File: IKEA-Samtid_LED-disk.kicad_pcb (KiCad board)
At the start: 2 copper layers, 100 x 100 mm, 70 parts

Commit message: Made schematic + placing a couple of LEDs.
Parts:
- removed C? (x2): VAL**, my_parts:MADW__C0805
- removed IC?: VAL**, my_parts:MADW__TQFP_32_7x7
- removed LED? (x63): VAL**, WS2812B:WS2812B_data-bridgeable
- removed P?: VAL**, my_parts:MADW__SIL-6
- removed X?: VAL**, my_parts:MADW__murata-resonator__CSTCE16M0V53-R0
- added C1: 100nF, my_parts:MADW__C0805, F.Cu at (186.0, 212.8)
- added C10: C, my_parts:MADW__C0805, F.Cu at (222.3, 182.1)
- added C11: C, my_parts:MADW__C0805, F.Cu at (237.5, 164.9)
- added C12: C, my_parts:MADW__C0805, F.Cu at (232.8, 170.3)
- added C13: C, my_parts:MADW__C0805, F.Cu at (245.2, 158.5)
- added C14: C, my_parts:MADW__C0805, F.Cu at (227.0, 175.7)
- added C15: C, my_parts:MADW__C0805, F.Cu at (210.0, 193.9)
- added C16: C, my_parts:MADW__C0805, F.Cu at (232.8, 163.9)
- added C17: C, my_parts:MADW__C0805, F.Cu at (217.6, 175.7)
- added C18: C, my_parts:MADW__C0805, F.Cu at (210.0, 187.5)
- added C19: C, my_parts:MADW__C0805, F.Cu at (245.2, 152.1)
- added C2: 1µF, my_parts:MADW__C0805, F.Cu at (193.3, 212.6)
- added C20: C, my_parts:MADW__C0805, F.Cu at (240.5, 158.5)
- added C21: C, my_parts:MADW__C0805, F.Cu at (224.1, 194.9)
- added C22: C, my_parts:MADW__C0805, F.Cu at (222.3, 175.7)
- added C23: C, my_parts:MADW__C0805, F.Cu at (240.5, 152.1)
- added C24: C, my_parts:MADW__C0805, F.Cu at (214.7, 194.9)
- added C25: C, my_parts:MADW__C0805, F.Cu at (227.0, 182.1)
- added C26: C, my_parts:MADW__C0805, F.Cu at (242.2, 164.9)
- added C27: C, my_parts:MADW__C0805, F.Cu at (237.5, 171.3)
- added C28: C, my_parts:MADW__C0805, F.Cu at (231.7, 176.7)
- added C29: C, my_parts:MADW__C0805, F.Cu at (219.4, 194.9)
- added C3: 100nF, my_parts:MADW__C0805, F.Cu at (186.0, 219.2)
- added C30: C, my_parts:MADW__C0805, F.Cu at (242.2, 171.3)
- added C31: C, my_parts:MADW__C0805, F.Cu at (217.6, 182.1)
- added C32: C, my_parts:MADW__C0805, F.Cu at (224.1, 188.5)
- added C33: C, my_parts:MADW__C0805, F.Cu at (231.7, 183.1)
- added C34: C, my_parts:MADW__C0805, F.Cu at (236.4, 177.8)
- added C35: C, my_parts:MADW__C0805, F.Cu at (241.1, 177.8)
- added C36: C, my_parts:MADW__C0805, F.Cu at (142.6, 57.9)
- added C37: C, my_parts:MADW__C0805, F.Cu at (339.0, 171.3)
- added C38: C, my_parts:MADW__C0805, F.Cu at (320.9, 189.6)
- added C39: C, my_parts:MADW__C0805, F.Cu at (302.1, 187.5)
- added C4: DNP, my_parts:MADW__C0805, F.Cu at (199.1, 205.2)
- added C40: C, my_parts:MADW__C0805, F.Cu at (316.2, 194.9)
- added C41: C, my_parts:MADW__C0805, F.Cu at (328.5, 184.2)
- added C42: C, my_parts:MADW__C0805, F.Cu at (333.2, 177.8)
- added C43: C, my_parts:MADW__C0805, F.Cu at (328.5, 177.8)
- added C44: C, my_parts:MADW__C0805, F.Cu at (323.8, 183.1)
- added C45: C, my_parts:MADW__C0805, F.Cu at (311.5, 188.5)
- added C46: C, my_parts:MADW__C0805, F.Cu at (332.5, 152.1)
- added C47: C, my_parts:MADW__C0805, F.Cu at (309.7, 175.7)
- added C48: C, my_parts:MADW__C0805, F.Cu at (324.9, 163.9)
- added C49: C, my_parts:MADW__C0805, F.Cu at (337.2, 152.1)
- added C5: C, my_parts:MADW__C0805, F.Cu at (150.0, 57.2)
- added C50: C, my_parts:MADW__C0805, F.Cu at (332.5, 158.5)
- added C51: C, my_parts:MADW__C0805, F.Cu at (314.4, 175.7)
- added C52: C, my_parts:MADW__C0805, F.Cu at (309.7, 182.1)
- added C53: C, my_parts:MADW__C0805, F.Cu at (302.1, 193.9)
- added C54: C, my_parts:MADW__C0805, F.Cu at (319.1, 175.7)
- added C55: C, my_parts:MADW__C0805, F.Cu at (337.2, 158.5)
- added C56: C, my_parts:MADW__C0805, F.Cu at (324.9, 170.3)
- added C57: C, my_parts:MADW__C0805, F.Cu at (329.6, 164.9)
- added C58: C, my_parts:MADW__C0805, F.Cu at (314.4, 182.1)
- added C59: C, my_parts:MADW__C0805, F.Cu at (306.8, 188.5)
- added C6: C, my_parts:MADW__C0805, F.Cu at (157.3, 57.9)
- added C60: C, my_parts:MADW__C0805, F.Cu at (306.8, 194.9)
- added C61: C, my_parts:MADW__C0805, F.Cu at (319.1, 182.1)
- added C62: C, my_parts:MADW__C0805, F.Cu at (334.3, 164.9)
- added C63: C, my_parts:MADW__C0805, F.Cu at (329.6, 171.3)
- added C64: C, my_parts:MADW__C0805, F.Cu at (323.8, 176.7)
- added C65: C, my_parts:MADW__C0805, F.Cu at (311.5, 194.9)
- added C66: C, my_parts:MADW__C0805, F.Cu at (334.3, 171.3)
- added C67: C, my_parts:MADW__C0805, F.Cu at (339.0, 164.9)
- added C68: C, my_parts:MADW__C0805, F.Cu at (316.2, 188.5)
- added C7: C, my_parts:MADW__C0805, F.Cu at (164.5, 59.7)
- added C8: C, my_parts:MADW__C0805, F.Cu at (219.4, 188.5)
- added C9: C, my_parts:MADW__C0805, F.Cu at (214.7, 188.5)
- added IC1: ATMEGA168PA-A, my_parts:MADW__TQFP_32_7x7, F.Cu at (168.4, 210.7)
- added JP1: AVR_ISP, my_parts:MADW__PIN_ARRAY_3x2_2.54mm, F.Cu at (179.2, 214.7)
- added LED1: WS2812B, WS2812B:WS2812B_data-bridgeable, F.Cu at (150.0, 50.0)
- added LED10: WS2812B, WS2812B:WS2812B_data-bridgeable, F.Cu at (198.7, 118.5)
- added LED11: WS2812B, WS2812B:WS2812B_data-bridgeable, F.Cu at (193.9, 130.0)
- added LED12: WS2812B, WS2812B:WS2812B_data-bridgeable, F.Cu at (186.7, 136.1)
- added LED13: WS2812B, WS2812B:WS2812B_data-bridgeable, F.Cu at (178.2, 138.4)
- added LED14: WS2812B, WS2812B:WS2812B_data-bridgeable, F.Cu at (169.7, 140.4)
- added LED15: WS2812B, WS2812B:WS2812B_data-bridgeable, F.Cu at (160.1, 143.9)
- added LED16: WS2812B, WS2812B:WS2812B_data-bridgeable, F.Cu at (150.0, 140.0)
- added LED17: WS2812B, WS2812B:WS2812B_data-bridgeable, F.Cu at (140.6, 143.1)
- added LED18: WS2812B, WS2812B:WS2812B_data-bridgeable, F.Cu at (132.5, 142.4)
- added LED19: WS2812B, WS2812B:WS2812B_data-bridgeable, F.Cu at (124.6, 138.4)
- added LED2: WS2812B, WS2812B:WS2812B_data-bridgeable, F.Cu at (158.8, 50.9)
- added LED20: WS2812B, WS2812B:WS2812B_data-bridgeable, F.Cu at (117.0, 134.3)
- added LED21: WS2812B, WS2812B:WS2812B_data-bridgeable, F.Cu at (109.7, 126.2)
- added LED22: WS2812B, WS2812B:WS2812B_data-bridgeable, F.Cu at (104.2, 117.9)
- added LED23: WS2812B, WS2812B:WS2812B_data-bridgeable, F.Cu at (100.6, 105.7)
- added LED24: WS2812B, WS2812B:WS2812B_data-bridgeable, F.Cu at (105.0, 95.0)
- added LED25: WS2812B, WS2812B:WS2812B_data-bridgeable, F.Cu at (101.2, 84.3)
- added LED26: WS2812B, WS2812B:WS2812B_data-bridgeable, F.Cu at (103.6, 72.7)
- added LED27: WS2812B, WS2812B:WS2812B_data-bridgeable, F.Cu at (111.6, 65.6)
- added LED28: WS2812B, WS2812B:WS2812B_data-bridgeable, F.Cu at (117.0, 57.5)
- added LED29: WS2812B, WS2812B:WS2812B_data-bridgeable, F.Cu at (123.5, 52.4)
- added LED3: WS2812B, WS2812B:WS2812B_data-bridgeable, F.Cu at (167.2, 53.4)
- added LED30: WS2812B, WS2812B:WS2812B_data-bridgeable, F.Cu at (131.1, 49.2)
- added LED31: WS2812B, WS2812B:WS2812B_data-bridgeable, F.Cu at (137.4, 40.7)
- added LED32: WS2812B, WS2812B:WS2812B_data-bridgeable, F.Cu at (141.3, 50.9)
- added LED33: WS2812B, WS2812B:WS2812B_data-bridgeable, F.Cu at (257.9, 178.5)
- added LED34: WS2812B, WS2812B:WS2812B_data-bridgeable, F.Cu at (265.5, 154.9)
- added LED35: WS2812B, WS2812B:WS2812B_data-bridgeable, F.Cu at (257.9, 166.7)
- added LED36: WS2812B, WS2812B:WS2812B_data-bridgeable, F.Cu at (280.7, 178.5)
- added LED37: WS2812B, WS2812B:WS2812B_data-bridgeable, F.Cu at (265.5, 190.3)
- added LED38: WS2812B, WS2812B:WS2812B_data-bridgeable, F.Cu at (295.9, 166.7)
- added LED39: WS2812B, WS2812B:WS2812B_data-bridgeable, F.Cu at (303.5, 166.7)
- added LED4: WS2812B, WS2812B:WS2812B_data-bridgeable, F.Cu at (175.0, 57.6)
- added LED40: WS2812B, WS2812B:WS2812B_data-bridgeable, F.Cu at (273.1, 190.3)
- added LED41: WS2812B, WS2812B:WS2812B_data-bridgeable, F.Cu at (288.3, 178.5)
- added LED42: WS2812B, WS2812B:WS2812B_data-bridgeable, F.Cu at (311.2, 154.9)
- added LED43: WS2812B, WS2812B:WS2812B_data-bridgeable, F.Cu at (280.7, 190.3)
- added LED44: WS2812B, WS2812B:WS2812B_data-bridgeable, F.Cu at (295.9, 178.5)
- added LED45: WS2812B, WS2812B:WS2812B_data-bridgeable, F.Cu at (311.2, 166.7)
- added LED46: WS2812B, WS2812B:WS2812B_data-bridgeable, F.Cu at (295.9, 190.3)
- added LED47: WS2812B, WS2812B:WS2812B_data-bridgeable, F.Cu at (318.8, 166.7)
- added LED48: WS2812B, WS2812B:WS2812B_data-bridgeable, F.Cu at (288.3, 190.3)
- added LED49: WS2812B, WS2812B:WS2812B_data-bridgeable, F.Cu at (326.4, 154.9)
- added LED5: WS2812B, WS2812B:WS2812B_data-bridgeable, F.Cu at (183.4, 65.0)
- added LED51: WS2812B, WS2812B:WS2812B_data-bridgeable, F.Cu at (318.8, 154.9)
- added LED52: WS2812B, WS2812B:WS2812B_data-bridgeable, F.Cu at (257.9, 154.9)
- added LED53: WS2812B, WS2812B:WS2812B_data-bridgeable, F.Cu at (273.1, 178.5)
- added LED54: WS2812B, WS2812B:WS2812B_data-bridgeable, F.Cu at (288.3, 166.7)
- added LED55: WS2812B, WS2812B:WS2812B_data-bridgeable, F.Cu at (280.7, 166.7)
- added LED56: WS2812B, WS2812B:WS2812B_data-bridgeable, F.Cu at (303.5, 154.9)
- added LED57: WS2812B, WS2812B:WS2812B_data-bridgeable, F.Cu at (295.9, 154.9)
- added LED58: WS2812B, WS2812B:WS2812B_data-bridgeable, F.Cu at (288.3, 154.9)
- added LED6: WS2812B, WS2812B:WS2812B_data-bridgeable, F.Cu at (189.6, 73.5)
- added LED60: WS2812B, WS2812B:WS2812B_data-bridgeable, F.Cu at (265.5, 178.5)
- added LED61: WS2812B, WS2812B:WS2812B_data-bridgeable, F.Cu at (273.1, 166.7)
- added LED62: WS2812B, WS2812B:WS2812B_data-bridgeable, F.Cu at (257.9, 190.3)
- added LED63: WS2812B, WS2812B:WS2812B_data-bridgeable, F.Cu at (265.5, 166.7)
- added LED64: WS2812B, WS2812B:WS2812B_data-bridgeable, F.Cu at (273.1, 154.9)
- added LED7: WS2812B, WS2812B:WS2812B_data-bridgeable, F.Cu at (194.1, 85.5)
- added LED8: WS2812B, WS2812B:WS2812B_data-bridgeable, F.Cu at (195.0, 95.0)
- added LED9: WS2812B, WS2812B:WS2812B_data-bridgeable, F.Cu at (203.8, 107.1)
- added P1: FTDI, my_parts:MADW__SIL-6, F.Cu at (183.0, 205.8)
- added P2: POWER, my_parts:MADW__SIL-2, F.Cu at (193.9, 205.8)
- added R1: 10k, my_parts:MADW__R0603_2, F.Cu at (190.7, 219.0)
- LED50: renamed from P?; value VAL** -> WS2812B; footprint my_parts:MADW__PIN_ARRAY_3x2_2.54mm -> WS2812B:WS2812B_data-bridgeable; moved to F.Cu
- LED59: renamed from LED?; value VAL** -> WS2812B; moved to F.Cu
- moved LED50 148.1 mm to (303.5, 178.5), turned to 0 degrees
- moved LED59 98.7 mm to (280.7, 154.9), turned to 0 degrees
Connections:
- LED50 pad 1: (no net) -> +5V
- LED50 pad 2: (no net) -> Net-(LED50-Pad2)
- LED50 pad 3: (no net) -> GND
- LED50 pad 4: (no net) -> Net-(LED49-Pad2)
- LED59 pad 1: (no net) -> +5V
- LED59 pad 2: (no net) -> Net-(LED59-Pad2)
- LED59 pad 3: (no net) -> GND
- LED59 pad 4: (no net) -> Net-(LED58-Pad2)
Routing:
- net GND: track 0.00 -> 44.7 mm
- net +5V: track 0.00 -> 20.5 mm
- net Net-(LED2-Pad2): track 0.00 -> 11.4 mm, vias 0 -> 2
- net Net-(LED1-Pad2): track 0.00 -> 11.2 mm, vias 0 -> 2
- net Net-(LED3-Pad2): track 0.00 -> 10.9 mm, vias 0 -> 2
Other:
- net class Default: clearance 0.254 -> 0.2032; trace_width 0.254 -> 0.4064; via_drill 0.635 -> 0.508
- rule trace_clearance: 0.254 -> 0.2032
- board text removed: "fix the angles!"

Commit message: First serious attempt at routing the board. No fun so far.
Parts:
- C1, C2, C3, C37, C38, C39, C4, C40, C68, IC1, JP1, LED33, LED34, LED35, LED36, LED37, LED38, LED39, LED40, LED41, LED64, P1, P2, R1: moved to B.Cu
- moved C37 220.8 mm to (150.0, 57.2), turned to 180 degrees
- moved C68 217.2 mm to (142.6, 57.9), turned to 191.3 degrees
- moved C38 209.9 mm to (157.4, 57.9), turned to 168.7 degrees
- moved C40 195.8 mm to (171.0, 63.6), turned to 146.7 degrees
- moved C39 187.6 mm to (164.4, 60.0), turned to 157.5 degrees
- moved LED64 167.9 mm to (141.3, 50.9), turned to 11.3 degrees
- moved LED33 167.7 mm to (150.0, 50.0)
- moved LED36 160.6 mm to (175.0, 57.6), turned to 326.2 degrees
- moved LED37 152.1 mm to (181.8, 63.2), turned to 315 degrees
- moved LED34 149.0 mm to (158.8, 50.9), turned to 348.7 degrees
- moved LED38 145.3 mm to (187.4, 70.0), turned to 303.8 degrees
- moved LED35 145.1 mm to (167.2, 53.4), turned to 337.5 degrees
- moved LED39 142.9 mm to (191.6, 77.8), turned to 292.4 degrees
- moved C8 134.0 mm to (171.0, 63.6), turned to 326.2 degrees
- moved LED40 130.6 mm to (194.1, 86.2), turned to 281.2 degrees
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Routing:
- net GND: track 44.7 -> 166.7 mm
- net +5V: track 20.5 -> 76.2 mm
- net Net-(LED39-Pad2): track 0.00 -> 20.2 mm, vias 0 -> 11
- net Net-(LED35-Pad2): track 0.00 -> 20.1 mm, vias 0 -> 10
- net Net-(LED33-Pad2): track 0.00 -> 19.7 mm, vias 0 -> 5
- net Net-(LED37-Pad2): track 0.00 -> 19.5 mm, vias 0 -> 10
- net /WS2812B-LEDs-1/D_OUT: track 0.00 -> 17.3 mm, vias 0 -> 1
- net Net-(LED36-Pad2): track 0.00 -> 17.1 mm
- net Net-(LED38-Pad2): track 0.00 -> 16.5 mm
- net /WS2812B-LEDs-2/E_OUT: track 0.00 -> 16.4 mm
- net Net-(LED34-Pad2): track 0.00 -> 16.2 mm
- net /WS2812B-LEDs-1/A_OUT: track 0.00 -> 11.3 mm, vias 0 -> 7
- net Net-(LED5-Pad2): track 0.00 -> 11.2 mm, vias 0 -> 5
- net Net-(LED4-Pad2): track 0.00 -> 11.1 mm, vias 0 -> 4
- net Net-(LED6-Pad2): track 0.00 -> 11.1 mm, vias 0 -> 4
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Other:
- net class Default: via_dia 0.889 -> 0.7112; via_drill 0.508 -> 0.3302
- rule via_min_drill: 0.508 -> 0.3302
- rule via_min_size: 0.889 -> 0.635

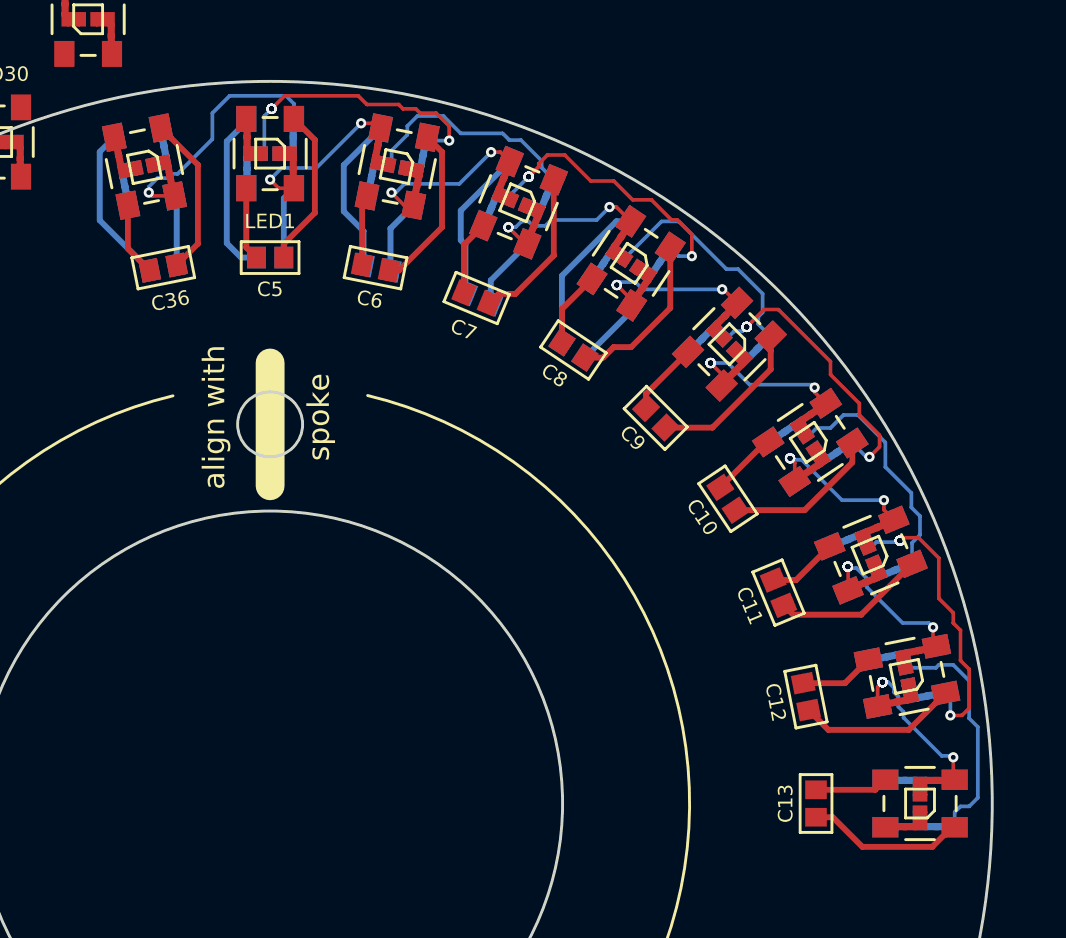
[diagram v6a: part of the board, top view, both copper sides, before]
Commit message: Rotate LEDs 90°. Might help with routing a bit.
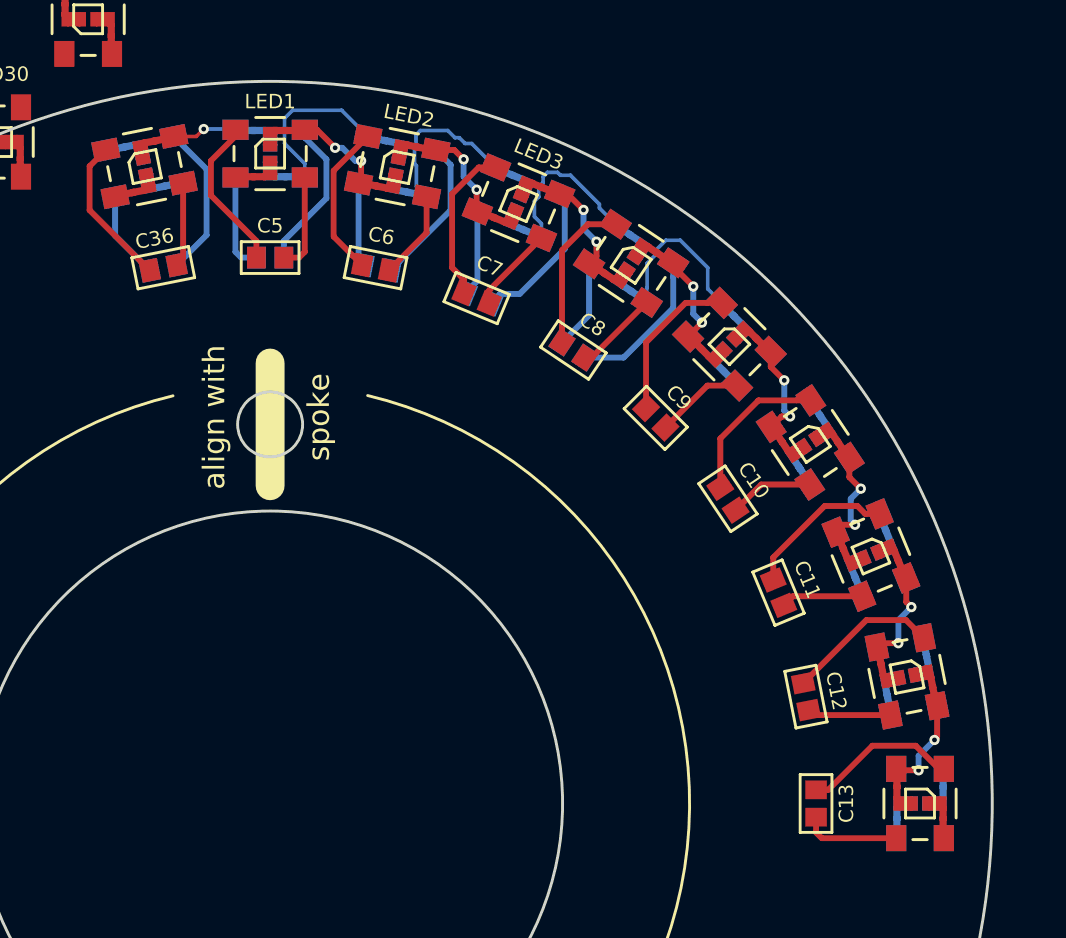
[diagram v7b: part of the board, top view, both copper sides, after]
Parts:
- turned C10 to 123.8 degrees
- turned C11 to 112.6 degrees
- turned C12 to 101.2 degrees
- turned C13 to 90 degrees
- turned C36 to 191.3 degrees
- turned C5 to 180 degrees
- turned C6 to 168.7 degrees
- turned C7 to 157.5 degrees
- turned C8 to 146.2 degrees
- turned C9 to 135 degrees
- turned LED1 to 270 degrees
- turned LED2 to 258.7 degrees
- turned LED3 to 247.5 degrees
- turned LED32 to 281.3 degrees
- turned LED33 to 90 degrees
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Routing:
- net +5V: track 76.2 -> 114.2 mm
- net GND: track 166.7 -> 138.5 mm
- net Net-(LED39-Pad2): track 20.2 -> 0.00 mm, vias 11 -> 0
- net Net-(LED37-Pad2): track 19.5 -> 0.00 mm, vias 10 -> 0
- net Net-(LED38-Pad2): track 16.5 -> 0.00 mm
- net /WS2812B-LEDs-2/E_OUT: track 16.4 -> 0.00 mm
- net /WS2812B-LEDs-1/D_OUT: track 17.3 -> 4.50 mm
- net Net-(LED35-Pad2): track 20.1 -> 11.5 mm, vias 10 -> 0
- net Net-(LED33-Pad2): track 19.7 -> 11.4 mm, vias 5 -> 0
- net Net-(LED36-Pad2): track 17.1 -> 11.4 mm
- net Net-(LED1-Pad2): track 12.0 -> 6.41 mm
- net Net-(LED2-Pad2): track 11.5 -> 6.19 mm
- net Net-(LED3-Pad2): track 11.5 -> 6.43 mm, vias 3 -> 2
- net Net-(LED34-Pad2): track 16.2 -> 11.4 mm
- net Net-(LED4-Pad2): track 11.1 -> 6.33 mm, vias 4 -> 2
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
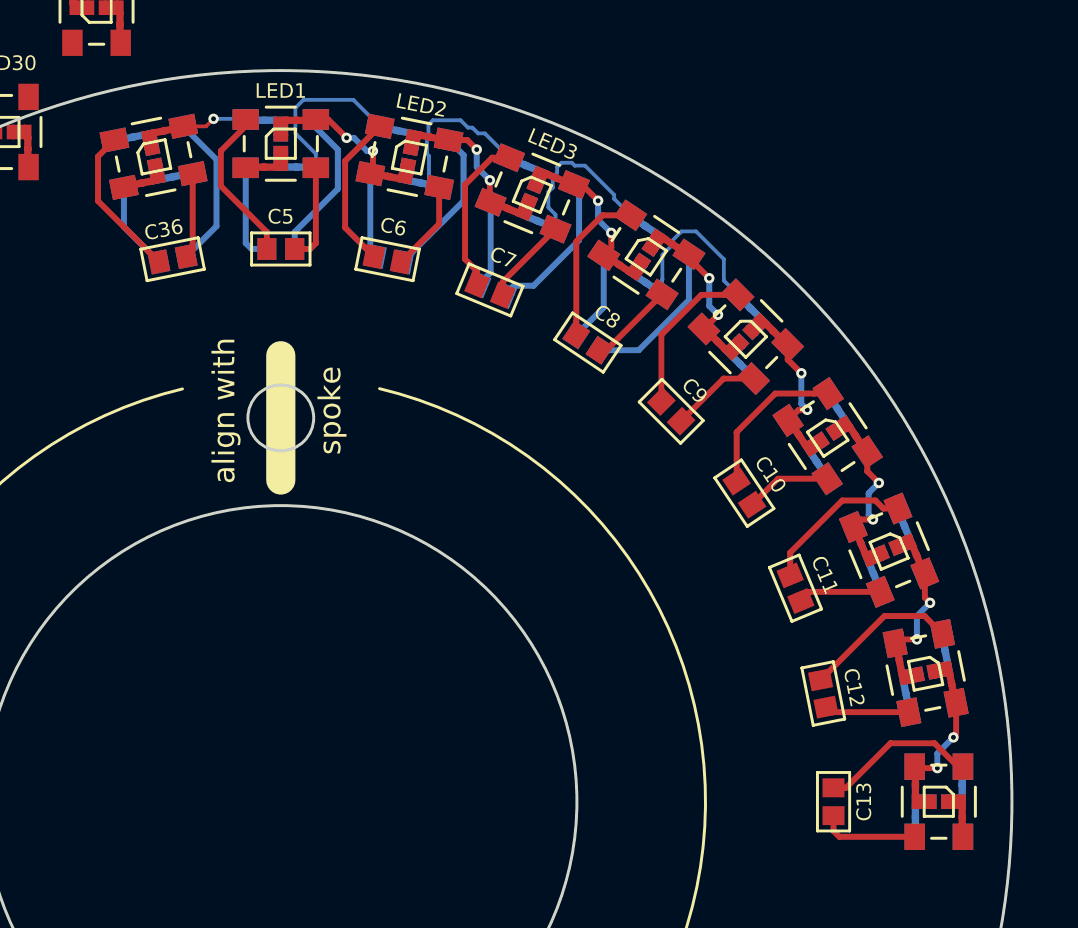
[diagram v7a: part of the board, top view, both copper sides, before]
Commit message: Limiting tracks to 45° is crap for circular boards. Looks horrible.
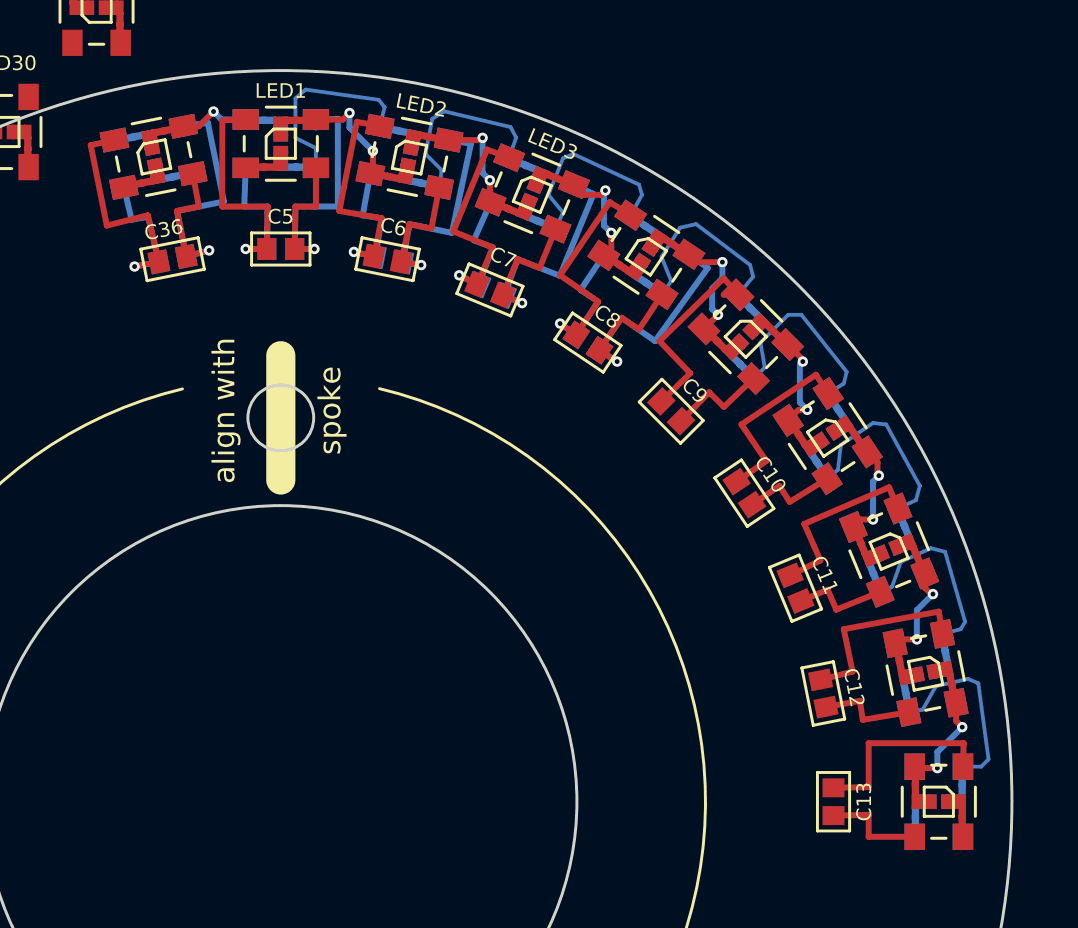
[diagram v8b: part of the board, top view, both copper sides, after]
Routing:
- net GND: track 138.5 -> 185.3 mm, vias 0 -> 5
- net +5V: track 114.2 -> 152.4 mm, vias 0 -> 5
- net Net-(LED37-Pad2): track 0.00 -> 13.5 mm
- net Net-(LED38-Pad2): track 0.00 -> 13.4 mm
- net /WS2812B-LEDs-2/E_OUT: track 0.00 -> 13.0 mm
- net Net-(LED39-Pad2): track 0.00 -> 12.8 mm
- net Net-(LED36-Pad2): track 11.4 -> 14.0 mm
- net Net-(LED33-Pad2): track 11.4 -> 13.6 mm
- net Net-(LED35-Pad2): track 11.5 -> 13.6 mm
- net Net-(LED34-Pad2): track 11.4 -> 13.1 mm
- net Net-(LED4-Pad2): track 6.33 -> 7.93 mm
- net Net-(LED3-Pad2): track 6.43 -> 7.46 mm
- net Net-(LED1-Pad2): track 6.41 -> 7.37 mm
- net Net-(LED2-Pad2): track 6.19 -> 7.02 mm
